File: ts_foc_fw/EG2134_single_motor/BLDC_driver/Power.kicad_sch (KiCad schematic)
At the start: 2 parts, among them U2 TPS5430DDAR

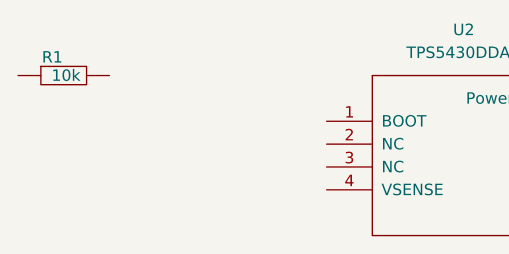
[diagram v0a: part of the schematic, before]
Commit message: add the cap c0603
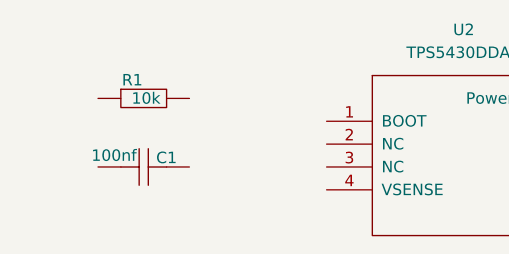
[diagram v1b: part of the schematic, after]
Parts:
- added C1: 100nf, BLDC_Drive_Tsfoc:C0603, symbol BLDC_Drive_Tsfoc:cap
- R1: footprint kicad_lceda:R0603 -> BLDC_Drive_Tsfoc:R0603
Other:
- moved on the sheet: R1
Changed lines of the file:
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@@
+	)
+	(symbol
+		(lib_id "BLDC_Drive_Tsfoc:cap")
+		(at 96.52 83.82 0)
+		(unit 1)
+		(exclude_from_sim no)
+		(in_bom yes)
+		(on_board yes)
+		(dnp no)
+		(property "Reference" "C1"
+			(at 99.06 82.804 0)
+			(effects
+				(font
+					(size 1.27 1.27)
+				)
+			)
+		)
+		(property "Value" "100nf"
+			(at 93.218 82.55 0)
+			(effects
+				(font
+					(size 1.27 1.27)
+				)
+			)
+		)
+		(property "Footprint" "BLDC_Drive_Tsfoc:C0603"
+			(at 96.774 85.344 0)
+			(effects
+				(font
+					(size 1.27 1.27)
+				)
+				(hide yes)
+			)
+		)
+		(property "Datasheet" ""
+			(at 96.52 89.408 0)
+			(effects
+				(font
+					(size 1.27 1.27)
+				)
+				(hide yes)
+			)
+		)
+		(property "Description" ""
+			(at 96.52 83.82 0)
+			(effects
+				(font
+					(size 1.27 1.27)
+				)
+				(hide yes)
+			)
+		)
+		(property "SuppliersPartNumber" "C519502"
+			(at 96.012 85.598 0)
+			(effects
+				(font
+					(size 1.27 1.27)
+				)
+				(hide yes)
+			)
+		)
+		(property "uuid" "std:d9d631d6bca44a2d934773ff44c148cf"
+			(at 96.012 85.598 0)
+			(effects
+				(font
+					(size 1.27 1.27)
+				)
+				(hide yes)
+			)
+		)
+		(pin "1"
+		)
+		(pin "2"
+		)
+		(instances
+			(project ""
+				(path "/3c13b5e1-57fa-4740-a1aa-c7a3ab53fab1/d172ac3e-1e62-4007-bb2b-f5b25040ec25"
+					(reference "C1")
+					(unit 1)
+				)
+			)
+		)
 	)
 	(symbol
 		(lib_id "BLDC_Drive_Tsfoc:res")
-		(at 87.63 73.66 0)
+		(at 96.52 76.2 0)
 		(unit 1)
 		(exclude_from_sim no)
@@
 		(dnp no)
 		(property "Reference" "R1"
-			(at 86.36 71.628 0)
+			(at 95.25 74.168 0)
 			(effects
 				(font
@@
 		)
 		(property "Value" "10k"
-			(at 87.884 73.66 0)
+			(at 96.774 76.2 0)
 			(effects
 				(font
@@
 			)
 		)
-		(property "Footprint" "kicad_lceda:R0603"
-			(at 87.63 75.184 0)
+		(property "Footprint" "BLDC_Drive_Tsfoc:R0603"
+			(at 96.52 77.724 0)
 			(effects
 				(font
@@
 		)
 		(property "Datasheet" "http://www.szlcsc.com/product/details_26547.html"
-			(at 88.138 76.454 0)
+			(at 97.028 78.994 0)
 			(effects
 				(font
@@
 		)
 		(property "Description" ""
-			(at 87.63 73.66 0)
+			(at 96.52 76.2 0)
 			(effects
 				(font
@@
 		)
 		(property "SuppliersPartNumber" "C25804"
-			(at 87.63 73.914 0)
+			(at 96.52 76.454 0)
 			(effects
 				(font
@@
 		)
 		(property "uuid" "std:b210af5a1436310a86e8b108e2e5a90b"
-			(at 87.122 75.946 0)
+			(at 96.012 78.486 0)
 			(effects
 				(font

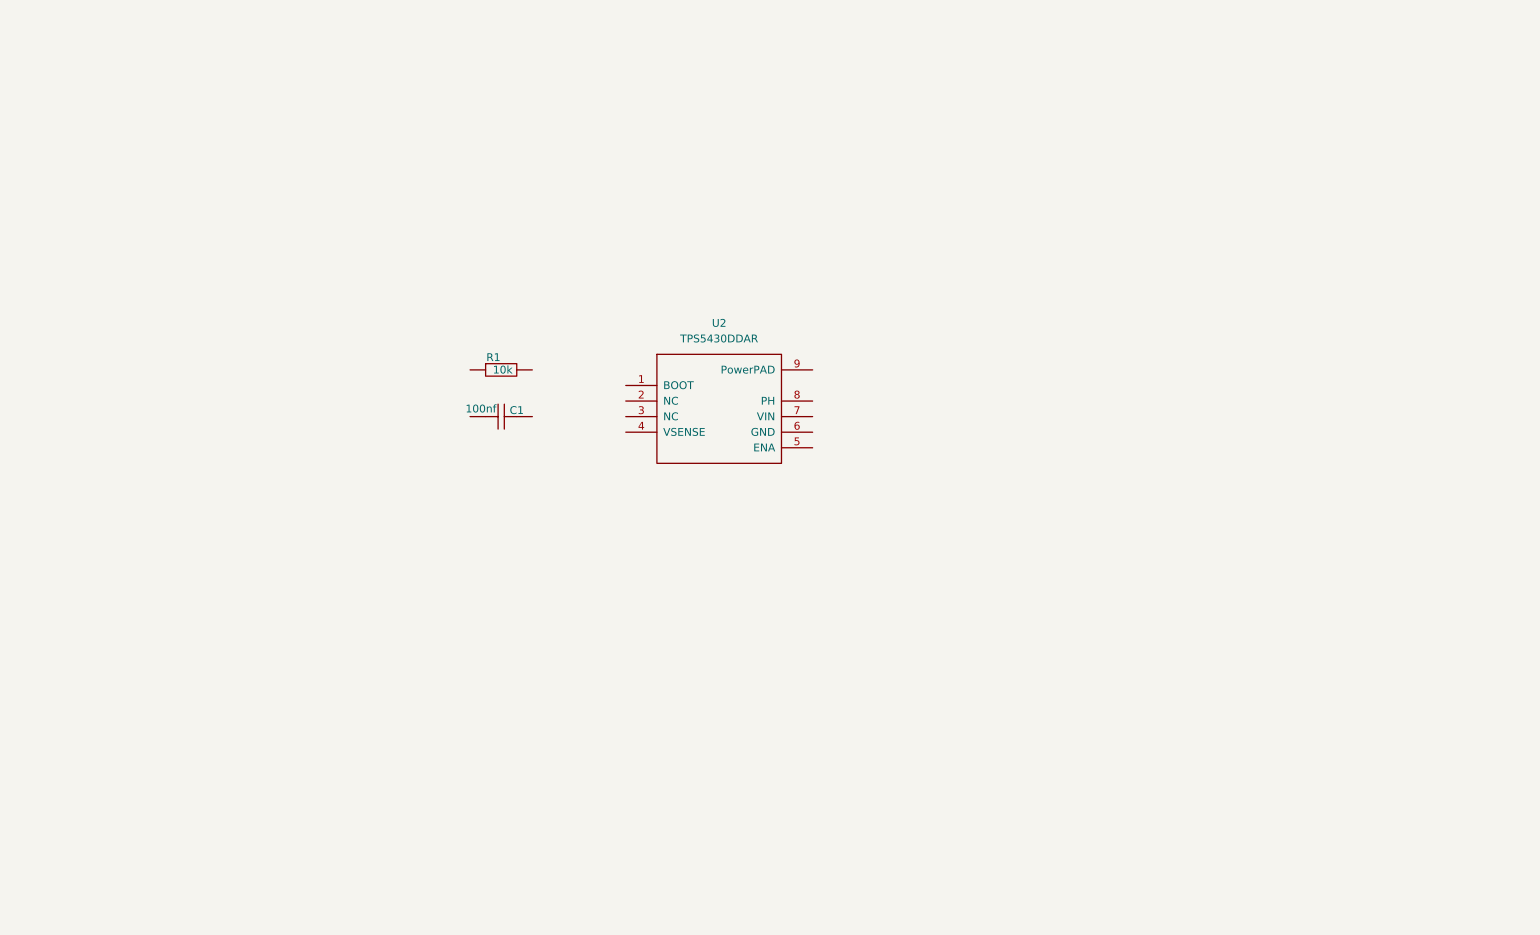
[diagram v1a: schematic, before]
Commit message: 原理图移植完成,PCB还没有布局
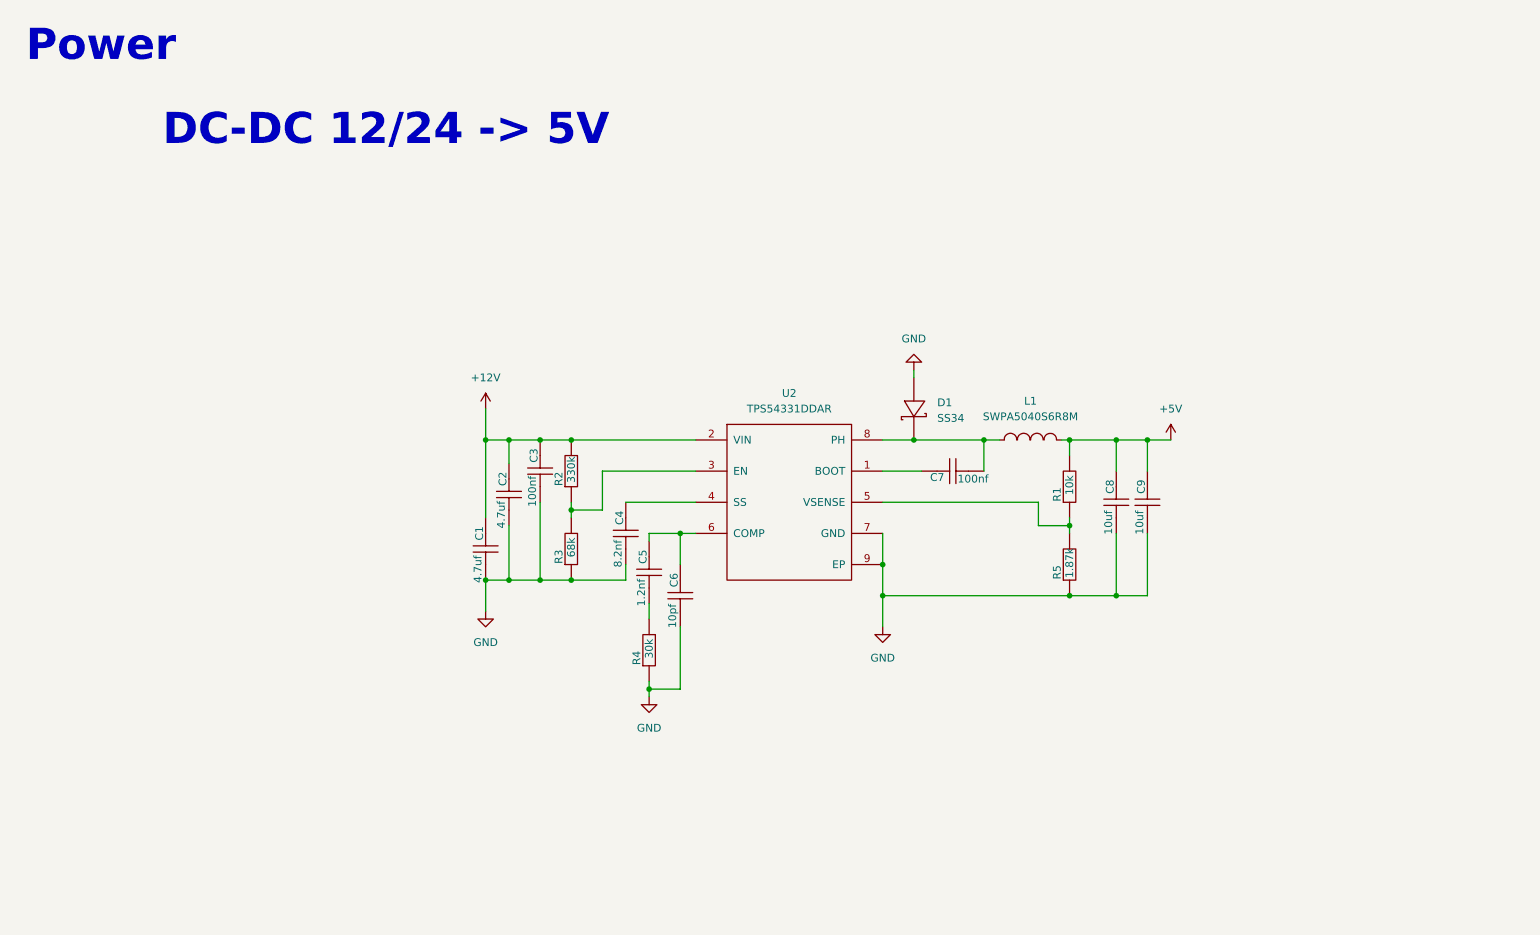
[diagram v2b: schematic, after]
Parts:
- removed U2: TPS5430DDAR, BLDC_Drive_Tsfoc:tps5430, symbol BLDC_Drive_Tsfoc:TPS5430DDAR
- added C2: 4.7uf, BLDC_Drive_Tsfoc:C0805, symbol BLDC_Drive_Tsfoc:cap
- added C3: 100nf, BLDC_Drive_Tsfoc:C0603, symbol BLDC_Drive_Tsfoc:cap
- added C4: 8.2nf, BLDC_Drive_Tsfoc:R0603, symbol BLDC_Drive_Tsfoc:cap
- added C5: 1.2nf, BLDC_Drive_Tsfoc:C0603, symbol BLDC_Drive_Tsfoc:cap
- added C6: 10pf, BLDC_Drive_Tsfoc:C0603, symbol BLDC_Drive_Tsfoc:cap
- added C7: 100nf, BLDC_Drive_Tsfoc:C0805, symbol BLDC_Drive_Tsfoc:cap
- added C8, C9: 10uf, BLDC_Drive_Tsfoc:C0805, symbol BLDC_Drive_Tsfoc:cap
- added D1: SS34, BLDC_Drive_Tsfoc:ss34, symbol BLDC_Drive_Tsfoc:SS34
- added L1: SWPA5040S6R8M, BLDC_Drive_Tsfoc:SWPA5040S6R8MT, symbol BLDC_Drive_Tsfoc:SWPA5040S6R8M
- added R2: 330k, BLDC_Drive_Tsfoc:R0603, symbol BLDC_Drive_Tsfoc:res
- added R3: 68k, BLDC_Drive_Tsfoc:R0603, symbol BLDC_Drive_Tsfoc:res
- added R4: 30k, BLDC_Drive_Tsfoc:R0603, symbol BLDC_Drive_Tsfoc:res
- added R5: 1.87k, BLDC_Drive_Tsfoc:R0603, symbol BLDC_Drive_Tsfoc:res
- added U2: TPS54331DDAR, BLDC_Drive_Tsfoc:tps54331, symbol BLDC_Drive_Tsfoc:TPS54331DDAR
- C1: value 100nf -> 4.7uf; footprint BLDC_Drive_Tsfoc:C0603 -> BLDC_Drive_Tsfoc:C0805
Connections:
- net GND: now reaches C1.1
- net GND: now also C2.1, C3.1, C4.1, C6.1, C8.1, C9.1, D1.2 (A), R3.1, R4.1, R5.1, U2.7 (GND), U2.9 (EP)
- net +12V: now reaches C1.2
- net +12V: now also C2.2, C3.2, R2.2, U2.2 (VIN)
- net at R1.1: now also R5.2, U2.5 (VSENSE)
- net +5V: now reaches R1.2
- net +5V: now also C8.2, C9.2, L1.2
- new net: C4.2, U2.4 (SS)
- new net: C7.1, D1.1 (K), L1.1, U2.8 (PH)
- new net: C7.2, U2.1 (BOOT)
- new net: R2.1, R3.2, U2.3 (EN)
- new net: C5.2, C6.2, U2.6 (COMP)
- new net: C5.1, R4.2
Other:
- note added: "DC-DC 12/24 -> 5V"
- note added: "Power"
- moved on the sheet: C1

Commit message: dayly
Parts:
- C4: footprint BLDC_Drive_Tsfoc:R0603 -> BLDC_Drive_Tsfoc:C0603
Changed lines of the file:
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@@
 			)
 		)
-		(property "Footprint" "BLDC_Drive_Tsfoc:R0603"
+		(property "Footprint" "BLDC_Drive_Tsfoc:C0603"
 			(at 118.364 102.616 0)
 			(effects

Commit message: 同步20241108_night
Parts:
- added C19, C22: 4.7uf, BLDC_Drive_Tsfoc:C0805, symbol BLDC_Drive_Tsfoc:cap
- added C20, C21: 100nf, BLDC_Drive_Tsfoc:C0603, symbol BLDC_Drive_Tsfoc:cap
- added U5: AMS1117-3.3(SOT-89), BLDC_Drive_Tsfoc:AMS11173v3-SOT-89, symbol BLDC_Drive_Tsfoc:AMS1117-3.3(SOT-89)
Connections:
- net +5V: now also C19.2, C20.2, U5.3 (Vin)
- net GND: now also C19.1, C20.1, C21.1, C22.1, U5.1 (GND)
- new net +3.3V: C21.2, C22.2, U5.2 (Vout)
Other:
- moved on the sheet: C1, C2, C3, C4, C5, C6, C7, C8, C9, D1, L1, R1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
